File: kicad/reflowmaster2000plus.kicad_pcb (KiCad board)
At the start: 2 copper layers, 20 parts, among them IC1 TLP3036, U1 TRIAC, U2 TLC2272

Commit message: [mod] updated schema&pcb
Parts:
- removed R3: R, R1
- removed RV2: POT, POT_CMS
- added P1: CONN_8, SIL-8, F.Cu at (156.8, 130.0)
- added P2: Toaster, 2PIN_6mm, F.Cu at (242.0, 123.0)
- added P3: 220V, 2PIN_6mm, F.Cu at (242.0, 147.5)
- D2: value ZENER -> BAT46; footprint D3 -> DO-35
- D3: value SCHOTTKY -> BZX55C5V1; footprint D3 -> DO-35
- D4: value SCHOTTKY -> VREFDIODE; footprint D3 -> TO92
- R1, R2, R4, R5, R6, R7: footprint R1 -> R3
- RV1, RV3: footprint POT_CMS -> SIL-3
- moved C2 121.2 mm to (162.8, 122.3), turned to 270 degrees
- moved C1 116.5 mm to (166.4, 122.3), turned to 270 degrees
- moved C3 111.8 mm to (170.2, 122.3), turned to 270 degrees
- moved R4 99.8 mm to (164.1, 143.1)
- moved D1 96.8 mm to (173.4, 143.1)
- moved IC1 82.3 mm to (183.4, 145.7), turned to 270 degrees
- moved RV1 80.4 mm to (171.3, 132.3)
- moved U1 80.0 mm to (197.6, 149.4), turned to 270 degrees
- moved D2 77.3 mm to (165.0, 136.3)
- moved R1 76.5 mm to (195.1, 143.1)
- moved R2 73.3 mm to (181.0, 132.3), turned to 180 degrees
- moved R7 71.0 mm to (191.8, 126.2)
- moved D3 69.3 mm to (165.0, 139.1), turned to 180 degrees
- moved R5 68.3 mm to (176.0, 136.3), turned to 0 degrees
- moved U2 66.6 mm to (191.8, 133.6), turned to 90 degrees
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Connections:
- net /1 renamed /+12V
- D2 pad 2: /vref -> /Uclamp
- D3 pad 1: (no net) -> GND
- D3 pad 2: (no net) -> /Uclamp
- D4 pad 2: (no net) -> N-000007
- IC1 pad 4: (no net) -> N-0000010
- R2 pad 1: N-0000020 -> N-000009
- R4 pad 1: (no net) -> /PWRctrl
- R6 pad 1: N-000003 (its old number) -> N-000007
- R7 pad 1: /I0 -> /KTYa
- RV1 pad 2: (no net) -> /Utemp
- RV3 pad 2: (no net) -> N-0000021
- RV3 pad 3: N-000005 -> N-0000021
- U1 pad 1: (no net) -> N-000006
- U1 pad 3: (no net) -> N-0000010
- U2 pad 1: N-000005 -> N-0000021
- U2 pad 2: /I0 -> N-000007
- U2 pad 3: N-000003 (its old number) -> /KTYa
- U2 pad 5: /I0 -> /KTYa
- U2 pad 6: (no net) -> N-000009
- U2 pad 7: N-0000020 -> N-000009
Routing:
- net N-0000017: track 0.00 -> 70.1 mm
- net N-000006: track 0.00 -> 54.4 mm
- net /KTYa: track 0.00 -> 49.3 mm
- net AGND: track 0.00 -> 24.5 mm
- net /Utemp: track 0.00 -> 22.9 mm
- net N-0000021: track 0.00 -> 18.6 mm
- net N-0000022: track 0.00 -> 16.1 mm
- net /+12V: track 0.00 -> 13.3 mm
- net N-000007: track 0.00 -> 12.8 mm
- net N-0000010: track 0.00 -> 9.15 mm
- net N-000001: track 0.00 -> 8.18 mm
- net /Uclamp: track 0.00 -> 7.11 mm
- net N-000009: track 0.00 -> 5.68 mm
- net /PWRctrl: track 0.00 -> 5.58 mm
- net N-000003: track 0.00 -> 4.87 mm
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- added copper zone on F.Cu, net GND
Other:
- net class hvpwr added: clearance 0.254, trace_width 1, via_dia 0.889, via_drill 0.635
- net class pwr added: clearance 0.254, trace_width 0.508, via_dia 0.889, via_drill 0.635

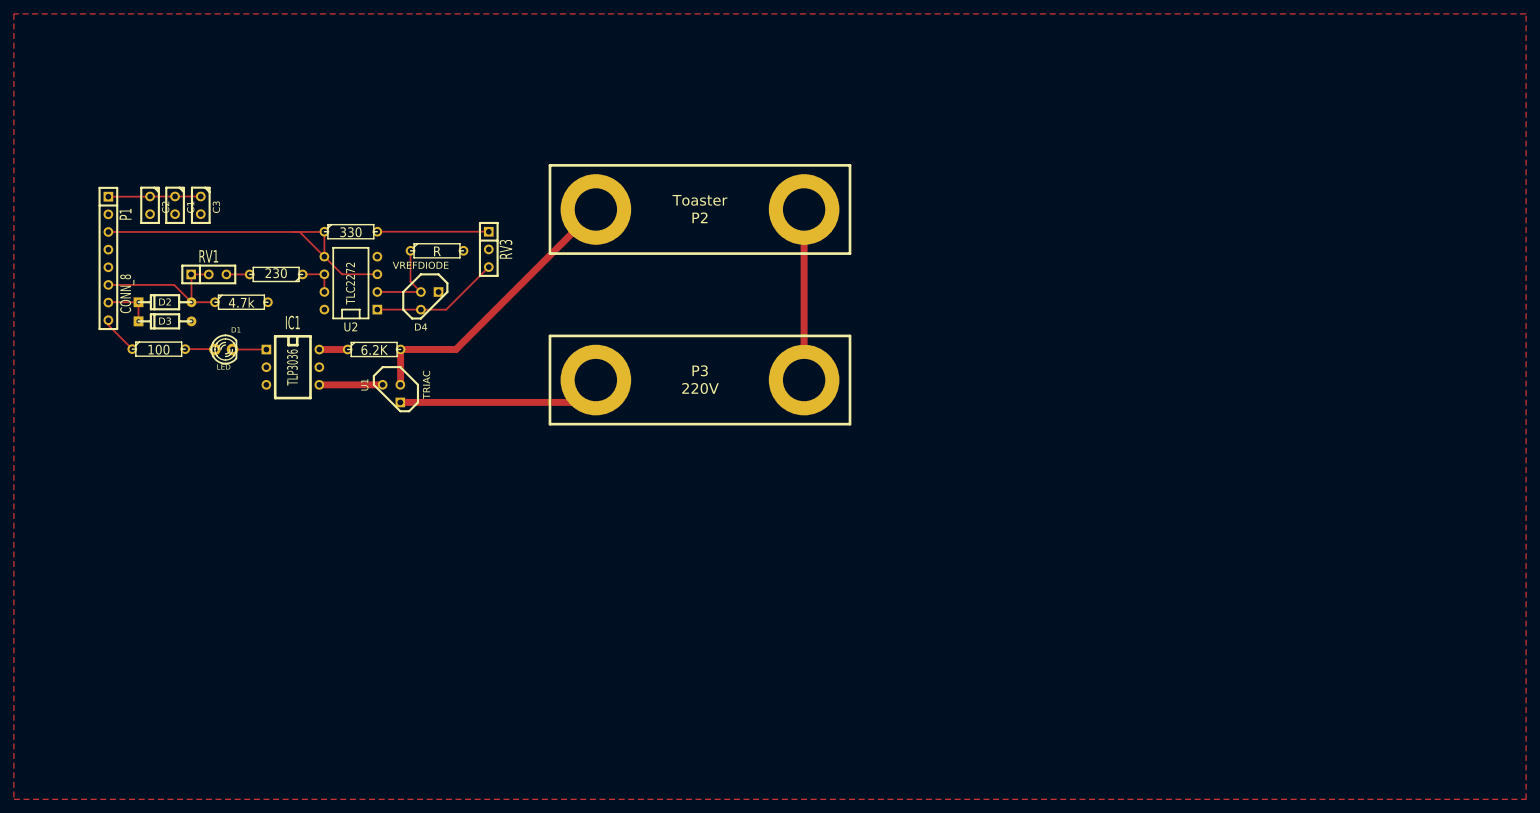
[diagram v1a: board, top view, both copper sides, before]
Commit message: [enh] compressed pcb into 5x2.5cm
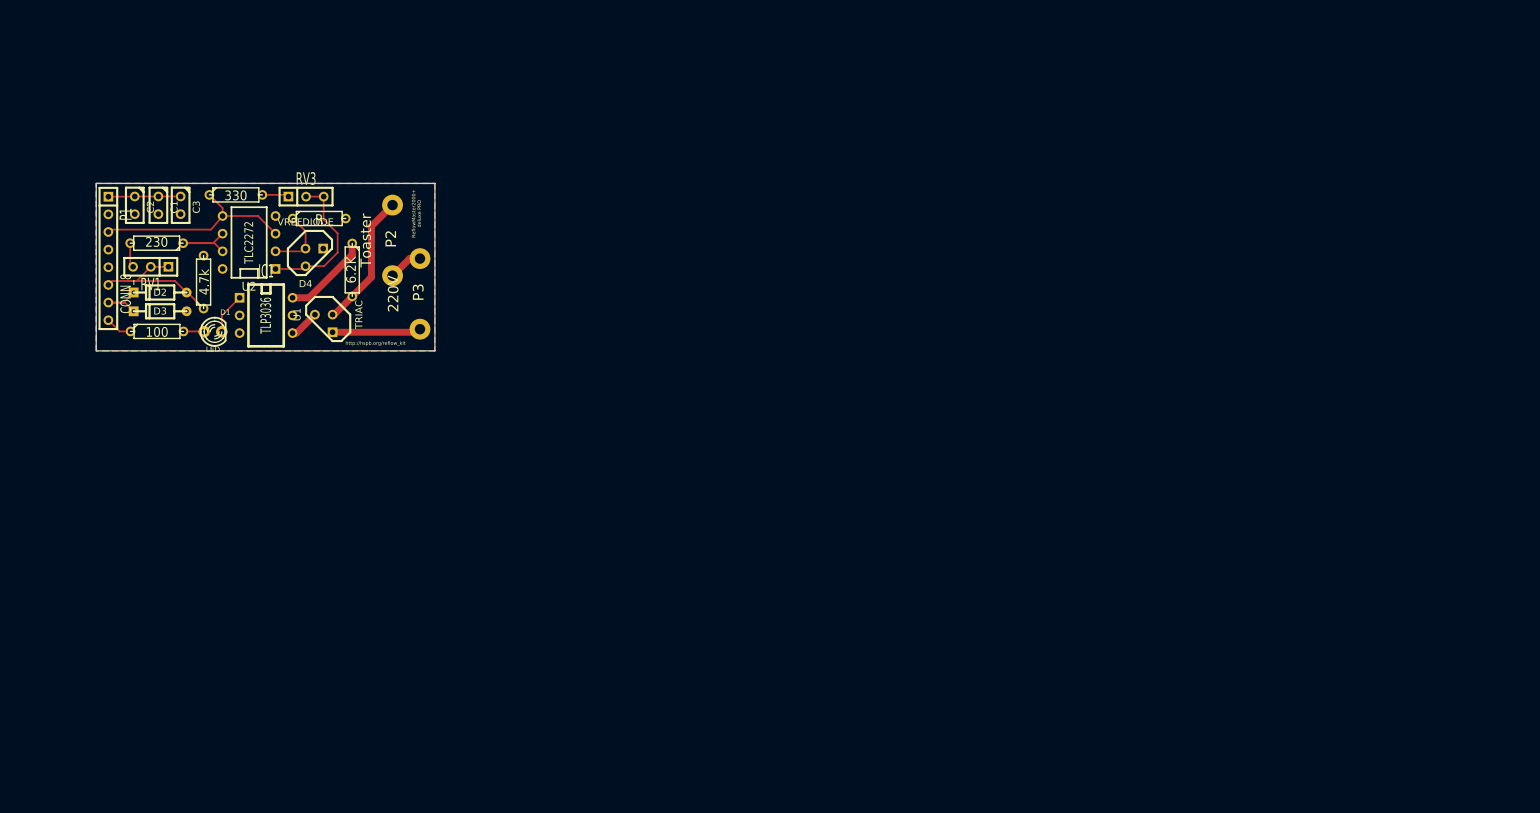
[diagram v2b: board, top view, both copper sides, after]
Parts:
- P2, P3: footprint 2PIN_6mm -> WireConnection_1-5mmDrill
- moved P2 44.5 mm to (197.8, 127.4), turned to 270 degrees
- moved P3 42.2 mm to (201.7, 135.1), turned to 270 degrees
- moved RV3 27.4 mm to (185.3, 121.1), turned to 0 degrees
- moved R2 17.8 mm to (163.8, 127.8)
- moved D4 17.7 mm to (186.5, 129.8)
- moved R6 17.6 mm to (187.2, 124.2)
- moved R7 17.4 mm to (175.2, 120.8)
- moved U2 15.8 mm to (177.1, 127.7)
- moved U1 14.0 mm to (187.8, 139.3)
- moved R1 11.9 mm to (191.9, 131.7), turned to 270 degrees
- moved RV1 8.42 mm to (162.9, 131.2), turned to 180 degrees
- moved IC1 8.39 mm to (179.6, 138.2)
- moved R5 6.17 mm to (170.6, 133.4), turned to 90 degrees
- moved D1 2.98 mm to (171.9, 140.6)
- moved C3 2.90 mm to (167.2, 122.3)
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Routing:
- net N-0000017: track 70.1 -> 19.6 mm
- net N-000006: track 54.4 -> 13.4 mm
- net /KTYa: track 49.3 -> 30.0 mm
- net AGND: track 24.5 -> 6.46 mm
- net N-0000022: track 16.1 -> 3.85 mm
- net N-000009: track 5.68 -> 12.4 mm
- net N-0000010: track 9.15 -> 4.36 mm
- net N-000001: track 8.18 -> 12.8 mm
- net N-000007: track 12.8 -> 9.57 mm
- net /+12V: track 13.3 -> 10.4 mm
- net N-0000021: track 18.6 -> 21.3 mm
- net /PWRctrl: track 5.58 -> 3.86 mm
- net /Uclamp: track 7.11 -> 8.40 mm
- net N-000002: track 4.29 -> 3.06 mm
- net N-000003: track 4.87 -> 5.95 mm
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- added copper zone on B.Cu, net GND
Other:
- board outline added: 48.8 x 24.1 mm
- board text added: "ReflowMaster2000+ deluxe PRO"
- board text added: "http://hspb.org/reflow_kit"

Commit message: [enh] lot's of polishing
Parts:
- C1: value C -> 10u
- C2: value C -> 100n
- C3: value C -> 10n
- IC1: value TLP3036 -> TLP3063
- R2: value 230 -> 330
- R4: value 100 -> 330
- R6: value R -> 10k
- RV1, RV3: value POT -> 500
- moved C1 14.4 mm to (163.8, 136.7)
- moved C3 14.4 mm to (167.1, 136.7)
- moved C2 14.4 mm to (160.5, 136.7)
- moved R2 5.96 mm to (163.5, 121.8)
- moved RV1 5.32 mm to (163.8, 126.0)
- moved D3 5.20 mm to (163.6, 132.4)
- moved D2 4.77 mm to (163.5, 130.2)
- moved R5 3.60 mm to (170.5, 129.8)
- moved P3 2.72 mm to (199.1, 134.5)
- moved P2 2.52 mm to (195.2, 127.0)
- moved RV3 2.49 mm to (187.4, 122.3)
- moved R6 2.43 mm to (188.5, 126.3)
- moved U1 1.80 mm to (188.8, 140.8), turned to 315 degrees
- moved R1 1.80 mm to (190.2, 132.2)
- moved D4 1.67 mm to (186.8, 131.5), turned to 45 degrees
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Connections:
- net AGND renamed GNDPWR
- C1 pad 1: /+12V -> +12V
- C2 pad 1: /+12V -> +12V
- C3 pad 1: /+12V -> +12V
- D2 pad 1: /Utemp -> /Uclamp
- D2 pad 2: /Uclamp -> /Utemp
- P1 pad 1: /+12V -> /KTYa
- P1 pad 3: /KTYa -> GND
- P1 pad 5: GND -> /Utemp
- P1 pad 6: /Utemp -> /Uclamp
- P1 pad 7: /Uclamp -> +12V
- U2 pad 4: (no net) -> GND
- U2 pad 8: (no net) -> +12V
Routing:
- net +12V: track 0.00 -> 19.9 mm
- net /+12V: track 10.4 -> 0.00 mm
- net N-000009: track 13.4 -> 8.93 mm
- net N-0000018: track 3.85 -> 7.55 mm
- net /Uclamp: track 8.40 -> 12.0 mm
- net /KTYa: track 30.0 -> 26.9 mm
- net N-000007: track 12.4 -> 10.6 mm
- net GNDPWR: track 6.46 -> 4.92 mm
- net N-0000012: track 3.57 -> 4.83 mm
- net N-000003: track 9.57 -> 10.7 mm
- net /Utemp: track 22.2 -> 21.3 mm
- net N-000002: track 5.95 -> 5.15 mm
- net N-0000011: track 4.36 -> 3.74 mm
- net N-0000016: track 21.3 -> 21.8 mm
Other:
- board size 48.8 x 24.1 mm -> 46.6 x 24.1 mm

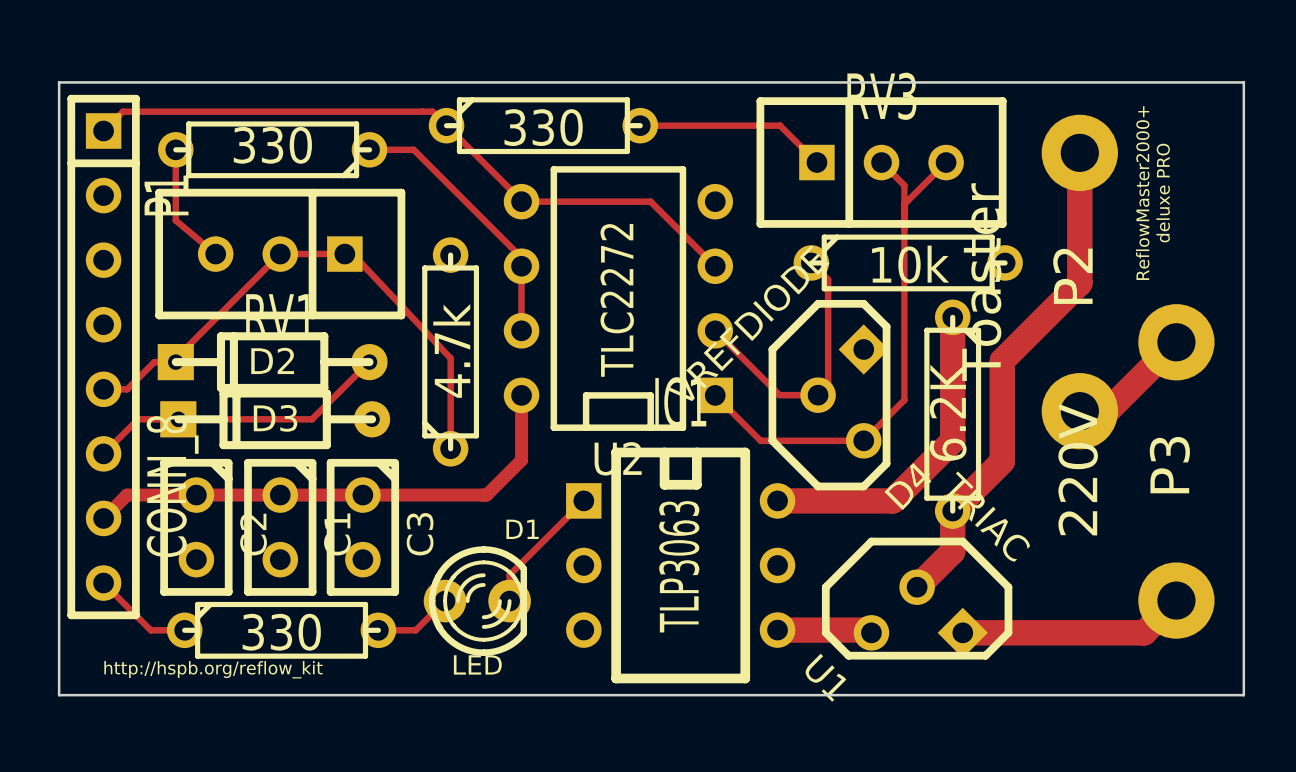
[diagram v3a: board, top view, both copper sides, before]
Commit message: [mod] moved fills, so they don't touch agnd
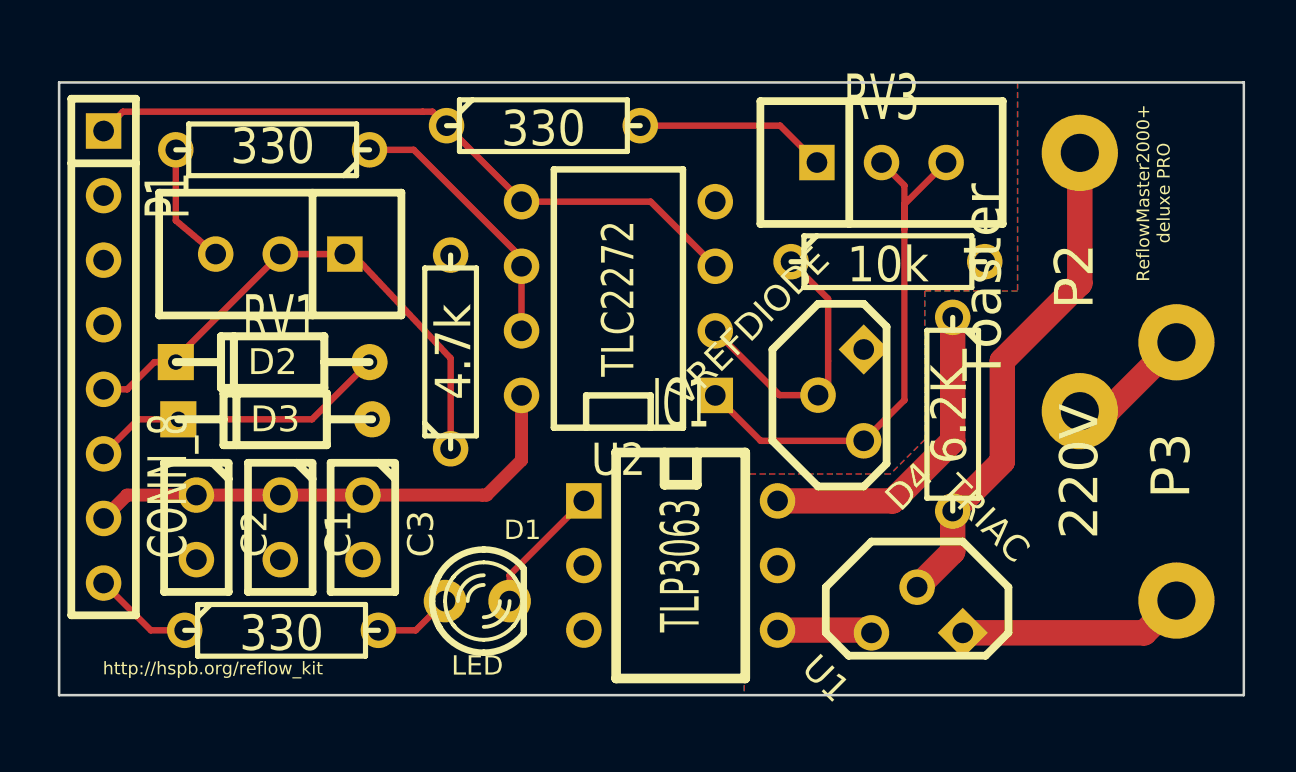
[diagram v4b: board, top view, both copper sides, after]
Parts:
- moved R6 0.80 mm to (187.7, 126.2)
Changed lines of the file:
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@@
     (links 41)
     (no_connects 0)
-    (area 155.049999 117.60825 215.999999 149.25)
+    (area 155.049999 118.50825 215.999999 149.25)
     (thickness 1.6)
     (drawings 8)
-    (tracks 76)
+    (tracks 77)
     (zones 0)
     (modules 21)
@@
   )
   (module R3 (layer F.Cu)
-    (at 188.5 126.3)
+    (at 187.7 126.25)
     (descr "Resitance 3 pas")
     (tags R)
@@
   (segment (start 159.69 121.85) (end 159.69 124.63) (width 0.254) (layer F.Cu) (net 10))
   (segment (start 188.35 124.95) (end 188.35 123.25) (width 0.254) (layer F.Cu) (net 11))
-  (segment (start 188.35 123.25) (end 187.45 122.35) (width 0.254) (layer F.Cu) (net 11) (status 800000))
-  (segment (start 186.75 133.296051) (end 188.35 131.696051) (width 0.254) (layer F.Cu) (net 11) (status 400000))
-  (segment (start 188.35 123.99) (end 189.99 122.35) (width 0.254) (layer F.Cu) (net 11) (status 800000))
+  (segment (start 188.35 123.25) (end 187.45 122.35) (width 0.254) (layer F.Cu) (net 11))
+  (segment (start 186.75 133.296051) (end 188.35 131.696051) (width 0.254) (layer F.Cu) (net 11))
+  (segment (start 188.35 123.99) (end 189.99 122.35) (width 0.254) (layer F.Cu) (net 11))
   (segment (start 188.35 131.696051) (end 188.35 124.95) (width 0.254) (layer F.Cu) (net 11))
   (segment (start 188.35 124.95) (end 188.35 123.99) (width 0.254) (layer F.Cu) (net 11))
@@
   (segment (start 188.85 139.053949) (end 190.25 137.653949) (width 1) (layer F.Cu) (net 12))
   (segment (start 190.25 137.653949) (end 190.25 136.06) (width 1) (layer F.Cu) (net 12) (status 20))
-  (segment (start 177.96 120.9) (end 183.46 120.9) (width 0.254) (layer F.Cu) (net 13) (status 400000))
-  (segment (start 183.46 120.9) (end 184.91 122.35) (width 0.254) (layer F.Cu) (net 13) (status 800000))
+  (segment (start 177.96 120.9) (end 183.46 120.9) (width 0.254) (layer F.Cu) (net 13))
+  (segment (start 183.46 120.9) (end 184.91 122.35) (width 0.254) (layer F.Cu) (net 13))
   (segment (start 172.82 139.6) (end 172.82 138.58) (width 0.254) (layer F.Cu) (net 14))
   (segment (start 172.82 138.58) (end 175.74 135.66) (width 0.254) (layer F.Cu) (net 14))
+  (segment (start 183.89 126.25) (end 185.35 127.71) (width 0.254) (layer F.Cu) (net 15))
+  (segment (start 185.35 127.71) (end 185.35 130.15) (width 0.254) (layer F.Cu) (net 15))
   (segment (start 184.953949 131.5) (end 185.35 131.103949) (width 0.254) (layer F.Cu) (net 15))
-  (segment (start 185.35 126.96) (end 184.69 126.3) (width 0.254) (layer F.Cu) (net 15))
-  (segment (start 185.35 131.103949) (end 185.35 126.96) (width 0.254) (layer F.Cu) (net 15))
+  (segment (start 185.35 131.103949) (end 185.35 130.15) (width 0.254) (layer F.Cu) (net 15))
   (segment (start 180.91 128.97) (end 183.44 131.5) (width 0.254) (layer F.Cu) (net 15))
   (segment (start 183.44 131.5) (end 184.953949 131.5) (width 0.254) (layer F.Cu) (net 15))
-  (segment (start 183.36 135.66) (end 187.89 135.66) (width 1) (layer F.Cu) (net 16) (status 400000))
+  (segment (start 183.36 135.66) (end 187.89 135.66) (width 1) (layer F.Cu) (net 16))
   (segment (start 187.89 135.66) (end 190.25 133.3) (width 1) (layer F.Cu) (net 16))
   (segment (start 190.25 133.3) (end 190.25 128.44) (width 1) (layer F.Cu) (net 16))
@@
     (polygon
       (pts
-        (xy 155.1 119.2) (xy 201.7 119.2) (xy 201.7 143.3) (xy 155.1 143.3)
+        (xy 155.1 119.2) (xy 192.8 119.2) (xy 192.8 127.4) (xy 189.15 127.4) (xy 189.15 133.25)
+        (xy 187.8 134.6) (xy 182.05 134.6) (xy 182.05 143.3) (xy 155.1 143.3)
       )
     )
@@
     (polygon
       (pts
-        (xy 155.1 143.3) (xy 155.1 119.2) (xy 201.7 119.2) (xy 201.7 143.3)
+        (xy 155.1 119.2) (xy 192.8 119.2) (xy 192.8 127.4) (xy 189.15 127.4) (xy 189.15 133.25)
+        (xy 187.8 134.6) (xy 182.05 134.6) (xy 182.05 143.3) (xy 155.1 143.3)
       )
     )

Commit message: [mod] removed my.lib from schema prefs
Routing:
- net N-000003: track 11.1 -> 9.20 mm
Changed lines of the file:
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@@
     (thickness 1.6)
     (drawings 8)
-    (tracks 77)
+    (tracks 75)
     (zones 0)
     (modules 21)
@@
   (segment (start 172.82 139.6) (end 172.82 138.58) (width 0.254) (layer F.Cu) (net 14))
   (segment (start 172.82 138.58) (end 175.74 135.66) (width 0.254) (layer F.Cu) (net 14))
-  (segment (start 183.89 126.25) (end 185.35 127.71) (width 0.254) (layer F.Cu) (net 15))
-  (segment (start 185.35 127.71) (end 185.35 130.15) (width 0.254) (layer F.Cu) (net 15))
-  (segment (start 184.953949 131.5) (end 185.35 131.103949) (width 0.254) (layer F.Cu) (net 15))
-  (segment (start 185.35 131.103949) (end 185.35 130.15) (width 0.254) (layer F.Cu) (net 15))
+  (segment (start 180.91 128.97) (end 181.17 128.97) (width 0.254) (layer F.Cu) (net 15) (status C00000))
+  (segment (start 181.17 128.97) (end 183.89 126.25) (width 0.254) (layer F.Cu) (net 15) (status C00000))
   (segment (start 180.91 128.97) (end 183.44 131.5) (width 0.254) (layer F.Cu) (net 15))
   (segment (start 183.44 131.5) (end 184.953949 131.5) (width 0.254) (layer F.Cu) (net 15))
